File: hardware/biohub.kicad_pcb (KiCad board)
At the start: 4 copper layers, 89 x 55 mm, 122 parts, among them J1 CONNECTOR, J2 Conn_02x13_Odd_Even, U1 **, U10 RM_10, U11 RM_10, U12 DCK6, U13 DCK6, U2 MCP2210-I_SS, U3 RI_16_1, U4 R_8, U5 ADP7142AUJZ-2.5-R7, U6 ADP7182AUJZ-2.5-R7, U7 ADS1299, U8 RM_10, U9 RM_10

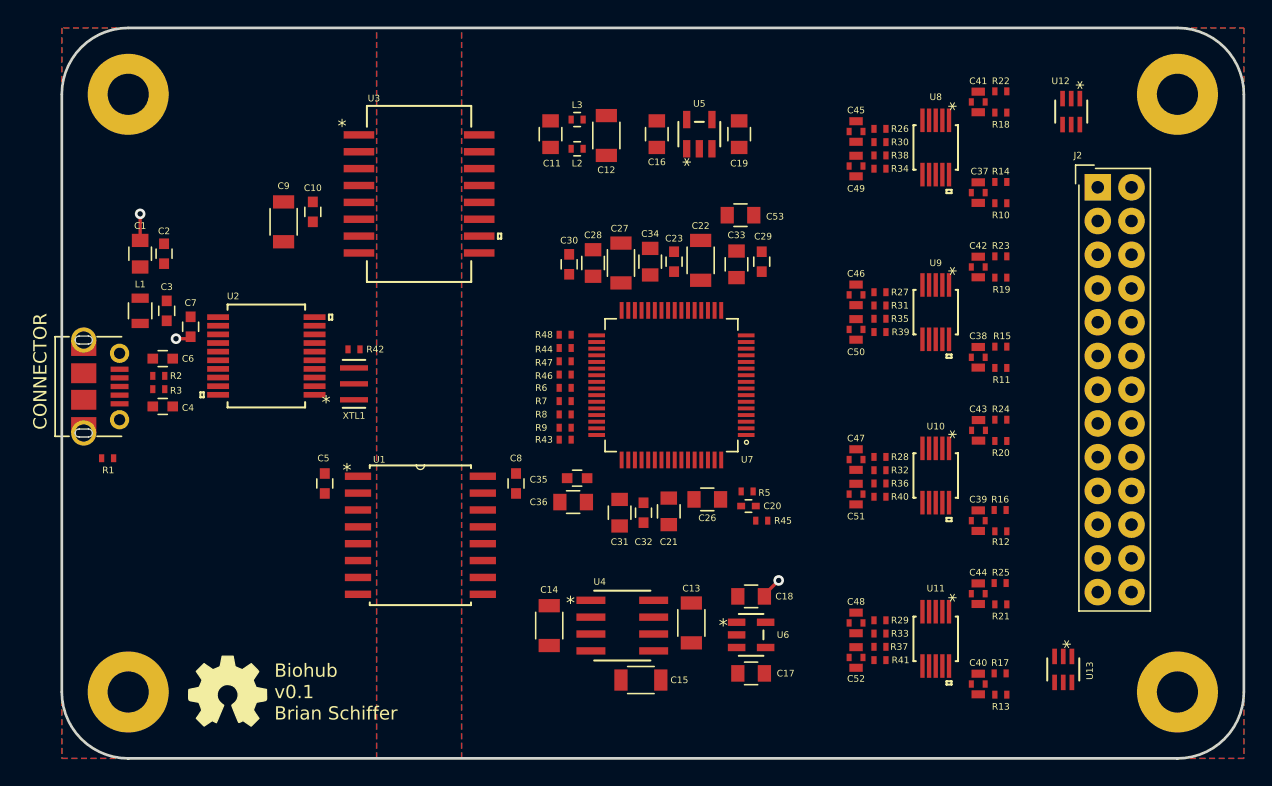
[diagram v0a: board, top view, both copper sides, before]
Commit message: Added 3.3V buck & started layout
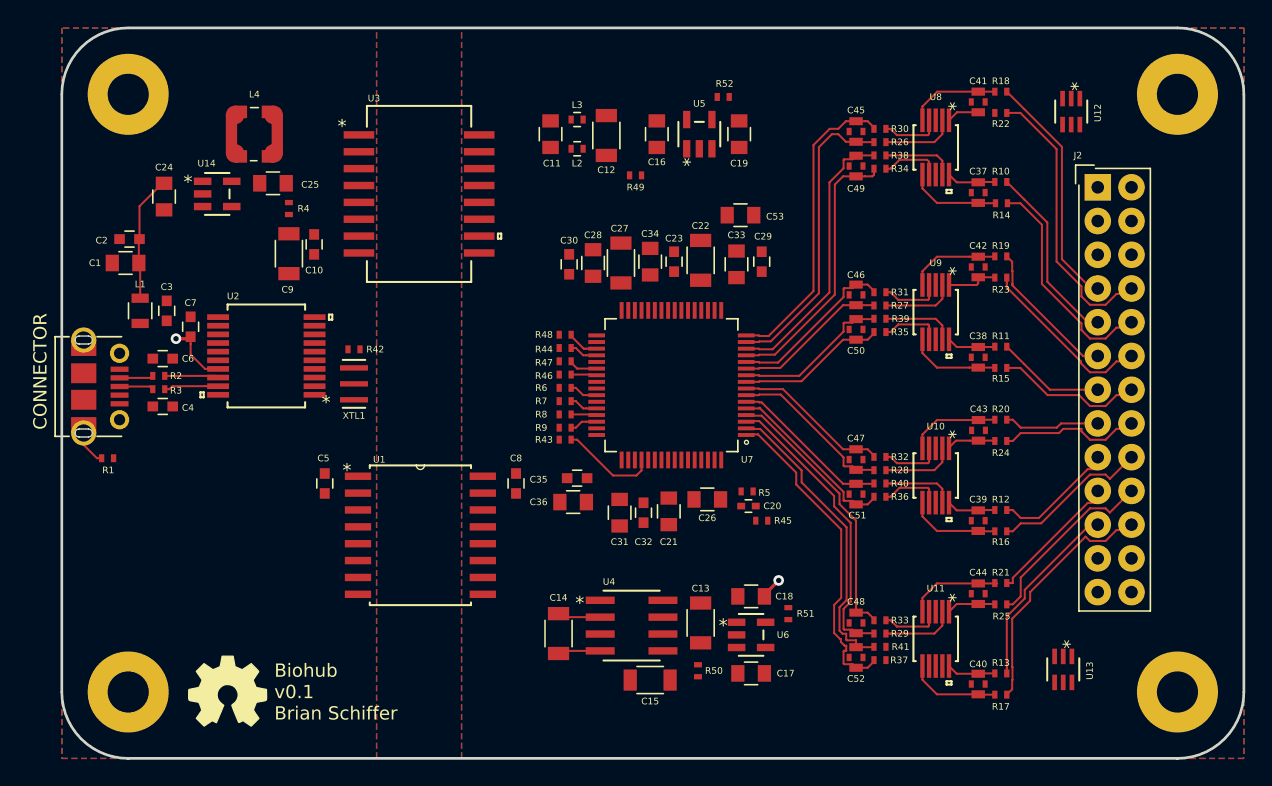
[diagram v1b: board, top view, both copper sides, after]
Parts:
- added C24: 4.7u, Capacitors_SMD:C_0805, F.Cu at (112.2, 77.7)
- added C25: 4.7u, Capacitors_SMD:C_0805, F.Cu at (120.4, 76.7)
- added L4: 4.7uH, biohub:L_Wuerth_WE-TPC, F.Cu at (119.0, 73.0)
- added R4: 0, Resistors_SMD:R_0402_NoSilk, F.Cu at (121.6, 78.6)
- added R49: 0, Resistors_SMD:R_0402_NoSilk, F.Cu at (147.7, 76.1)
- added R50: 0, Resistors_SMD:R_0402_NoSilk, F.Cu at (152.4, 113.4)
- added R51: 0, Resistors_SMD:R_0402_NoSilk, F.Cu at (159.2, 109.1)
- added R52: 0, Resistors_SMD:R_0402_NoSilk, F.Cu at (154.3, 70.2)
- added U14: MCP1603T-330I, biohub:MCP1603T-330I, F.Cu at (116.2, 77.5)
- U1: value ** -> ADUM1412BRWZ
- U10, U11, U8, U9: value RM_10 -> AD8244BRMZ
- U12, U13: value DCK6 -> TPD4E1B06DCKR; footprint biohub:TPD4E1B06DCKR -> TPD4E1B06DCKR
- U3: value RI_16_1 -> ADUM6020
- U4: value R_8 -> ADM8660ARZ
- U7: value ADS1299 -> ADS1299IPAG
- XTL1: value CSTCE -> CSTNE12M0GH5L000R0
- moved C2 2.82 mm to (109.6, 80.9), turned to 180 degrees
- moved C10 2.45 mm to (123.5, 81.3)
- moved C9 2.43 mm to (121.6, 82.0)
- moved R22 1.63 mm to (175.2, 71.4)
- moved R14 1.60 mm to (175.2, 78.2)
- moved R16 1.60 mm to (175.2, 102.9)
- moved R17 1.60 mm to (175.2, 115.2)
- moved R25 1.60 mm to (175.2, 108.4)
- moved R10 1.60 mm to (175.2, 76.6)
- moved R12 1.60 mm to (175.2, 101.3)
- moved R13 1.60 mm to (175.2, 113.6)
- moved R21 1.60 mm to (175.2, 106.8)
- moved R11 1.60 mm to (175.2, 89.0)
- moved R15 1.60 mm to (175.2, 90.6)
- moved R19 1.60 mm to (175.2, 82.2)
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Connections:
- C10 pad 1: VBUS -> VCOM
- C12 pad 1: +3V3 -> Net-(C12-Pad1)
- C45 pad 1: /interface/1P -> /interface/1N
- C45 pad 2: /interface/1N -> /interface/1P
- C46 pad 1: /interface/3P -> /interface/3N
- C46 pad 2: /interface/3N -> /interface/3P
- C47 pad 1: /interface/5P -> /interface/5N
- C47 pad 2: /interface/5N -> /interface/5P
- C48 pad 1: /interface/7P -> /interface/7N
- C48 pad 2: /interface/7N -> /interface/7P
- C49 pad 1: /interface/2P -> /interface/2N
- C49 pad 2: /interface/2N -> /interface/2P
- C50 pad 1: /interface/4P -> /interface/4N
- C50 pad 2: /interface/4N -> /interface/4P
- C51 pad 1: /interface/6P -> /interface/6N
- C51 pad 2: /interface/6N -> /interface/6P
- C52 pad 1: /interface/8P -> /interface/8N
- C52 pad 2: /interface/8N -> /interface/8P
- C9 pad 1: VBUS -> VCOM
- J2 pad 10: /interface/2N -> /interface/CONN_2N
- J2 pad 11: /interface/3P -> /interface/CONN_3P
- J2 pad 12: /interface/3N -> /interface/CONN_3N
- J2 pad 13: /interface/4P -> /interface/CONN_4P
- J2 pad 14: /interface/4N -> /interface/CONN_4N
- J2 pad 15: /interface/5P -> /interface/CONN_5P
- J2 pad 16: /interface/5N -> /interface/CONN_5N
- J2 pad 17: /interface/6P -> /interface/CONN_6P
- J2 pad 18: /interface/6N -> /interface/CONN_6N
- J2 pad 19: /interface/7P -> /interface/CONN_7P
- J2 pad 20: /interface/7N -> /interface/CONN_7N
- J2 pad 21: /interface/8P -> /interface/CONN_8P
- J2 pad 22: /interface/8N -> /interface/CONN_8N
- J2 pad 7: /interface/1P -> /interface/CONN_1P
- J2 pad 8: /interface/1N -> /interface/CONN_1N
- J2 pad 9: /interface/2P -> /interface/CONN_2P
- L2 pad 2: +3V3 -> Net-(C12-Pad1)
- R10 pad 2: /interface/2N -> /interface/CONN_2P
- R11 pad 2: /interface/4N -> /interface/CONN_4P
- R12 pad 2: /interface/6N -> /interface/CONN_6P
- R13 pad 2: /interface/8N -> /interface/CONN_8P
- R14 pad 2: /interface/2P -> /interface/CONN_2N
- R15 pad 2: /interface/4P -> /interface/CONN_4N
- R16 pad 2: /interface/6P -> /interface/CONN_6N
- R17 pad 2: /interface/8P -> /interface/CONN_8N
- R18 pad 2: /interface/1N -> /interface/CONN_1P
- R19 pad 2: /interface/3N -> /interface/CONN_3P
- R20 pad 2: /interface/5N -> /interface/CONN_5P
- R21 pad 2: /interface/7N -> /interface/CONN_7P
- R22 pad 2: /interface/1P -> /interface/CONN_1N
- R23 pad 2: /interface/3P -> /interface/CONN_3N
- R24 pad 2: /interface/5P -> /interface/CONN_5N
- R25 pad 2: /interface/7P -> /interface/CONN_7N
- R26 pad 1: /interface/1P -> /interface/1N
- R27 pad 1: /interface/3P -> /interface/3N
- R28 pad 1: /interface/5P -> /interface/5N
- R29 pad 1: /interface/7P -> /interface/7N
- R30 pad 1: /interface/1N -> /interface/1P
- R31 pad 1: /interface/3N -> /interface/3P
- R32 pad 1: /interface/5N -> /interface/5P
- R33 pad 1: /interface/7N -> /interface/7P
- R34 pad 1: /interface/2P -> /interface/2N
- R35 pad 1: /interface/4P -> /interface/4N
- R36 pad 1: /interface/6P -> /interface/6N
- R37 pad 1: /interface/8P -> /interface/8N
- R38 pad 1: /interface/2N -> /interface/2P
- R39 pad 1: /interface/4N -> /interface/4P
- R40 pad 1: /interface/6N -> /interface/6P
- R41 pad 1: /interface/8N -> /interface/8P
- U3 pad 5: VBUS -> VCOM
- U4 pad 5: -3V3 -> Net-(R50-Pad1)
- U5 pad 4: +2V5 -> Net-(R52-Pad1)
- U5 pad 5: +2V5 -> Net-(R52-Pad1)
- U6 pad 5: -2V5 -> Net-(R51-Pad1)
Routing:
- net /interface/8N: track 0.00 -> 24.4 mm
- net /interface/1P: track 0.00 -> 23.1 mm
- net /interface/8P: track 0.00 -> 22.9 mm
- net /interface/1N: track 0.00 -> 22.8 mm
- net /interface/7N: track 0.00 -> 22.2 mm
- net /interface/CONN_1N: track 0.00 -> 21.3 mm
- net /interface/2P: track 0.00 -> 20.9 mm
- net /interface/7P: track 0.00 -> 20.6 mm
- net /interface/2N: track 0.00 -> 20.6 mm
- net /interface/CONN_8N: track 0.00 -> 18.5 mm
- net /interface/CONN_1P: track 0.00 -> 17.9 mm
- net /interface/CONN_2N: track 0.00 -> 17.0 mm
- net /interface/CONN_8P: track 0.00 -> 14.4 mm
- net /interface/CONN_7N: track 0.00 -> 14.0 mm
- net /interface/CONN_2P: track 0.00 -> 13.8 mm
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- added copper zone on In2.Cu, net +2V5
- added copper zone on B.Cu, net -2V5
- added copper zone on In1.Cu, net GND
- removed copper zone on In1.Cu, net +2V5
- removed copper zone on In2.Cu, net -2V5
- removed copper zone on B.Cu, net GND
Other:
- net class Default: clearance 0.2 -> 0.1524; trace_width 0.25 -> 0.1524; via_dia 0.8 -> 0.6858; via_drill 0.4 -> 0.3302
- rule trace_clearance: 0.2 -> 0.1524
- rule trace_min: 0.2 -> 0.1524
- rule via_min_drill: 0.3 -> 0.254
- rule via_min_size: 0.4 -> 0.508
